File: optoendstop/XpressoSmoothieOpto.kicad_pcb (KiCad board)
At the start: 2 copper layers, 99.7 x 99.7 mm, 121 parts, among them J1 HEADER_4, J10 HEADER_3X2, J11 Pwr_in, J12 HEADER_4, J13 HEADER_4X2, J14 HEADER_3X2, J15 HEADER_4, J16 HEADER_4, J17 HEADER_4, J18 HEADER_4, J19 HEADER_2, J2 HEADER_4, J20 HEADER_2, J21 HEADER_2, J22 HEADER_2, J23 HEADER_4, J24 HEADER_4, J25 HEADER_4, J26 USB, J27 HEADER_4, J28 MICROSD-MOLEX, J3 HEADER_3, J4 HEADER_3X2, J5 HEADER_3X2, J6 LPCXPRESSO_GENERIC_HEADER, J7 HEADER_4, J8 HEADER_4, J9 HEADER_3X2, M1 LOGO_OSHW, M2 LOGO_OSHW, Q1 IRLB 8743, Q2 IRLB 8743, Q3 IRLB 8743, Q4 IRLB 8743, SW1 SW_PUSH, SW2 SW_PUSH, U1 POLOLU_A4988, U10 TC4422A, U11 TC4422A, U12 LM1117-3.3, U2 POLOLU_A4988, U3 POLOLU_A4988, U4 POLOLU_A4988, U5 POLOLU_A4988, U7 LM7809CT, U8 TC4422A, U9 TC4422A

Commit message: endstops_mod
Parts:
- moved C8 11.1 mm to (65.1, 117.5)
- moved C1 2.86 mm to (75.2, 117.5)
- moved J23 0.32 mm to (86.4, 109.5)
- moved J25 0.32 mm to (86.4, 113.3)
- moved J17 0.32 mm to (86.4, 105.7)
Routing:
- net Vin_rmot: track 317.8 -> 325.1 mm
- net GND: track 759.1 -> 755.0 mm
- net ZMIN: track 24.3 -> 23.5 mm
- net YMIN: track 25.8 -> 26.5 mm

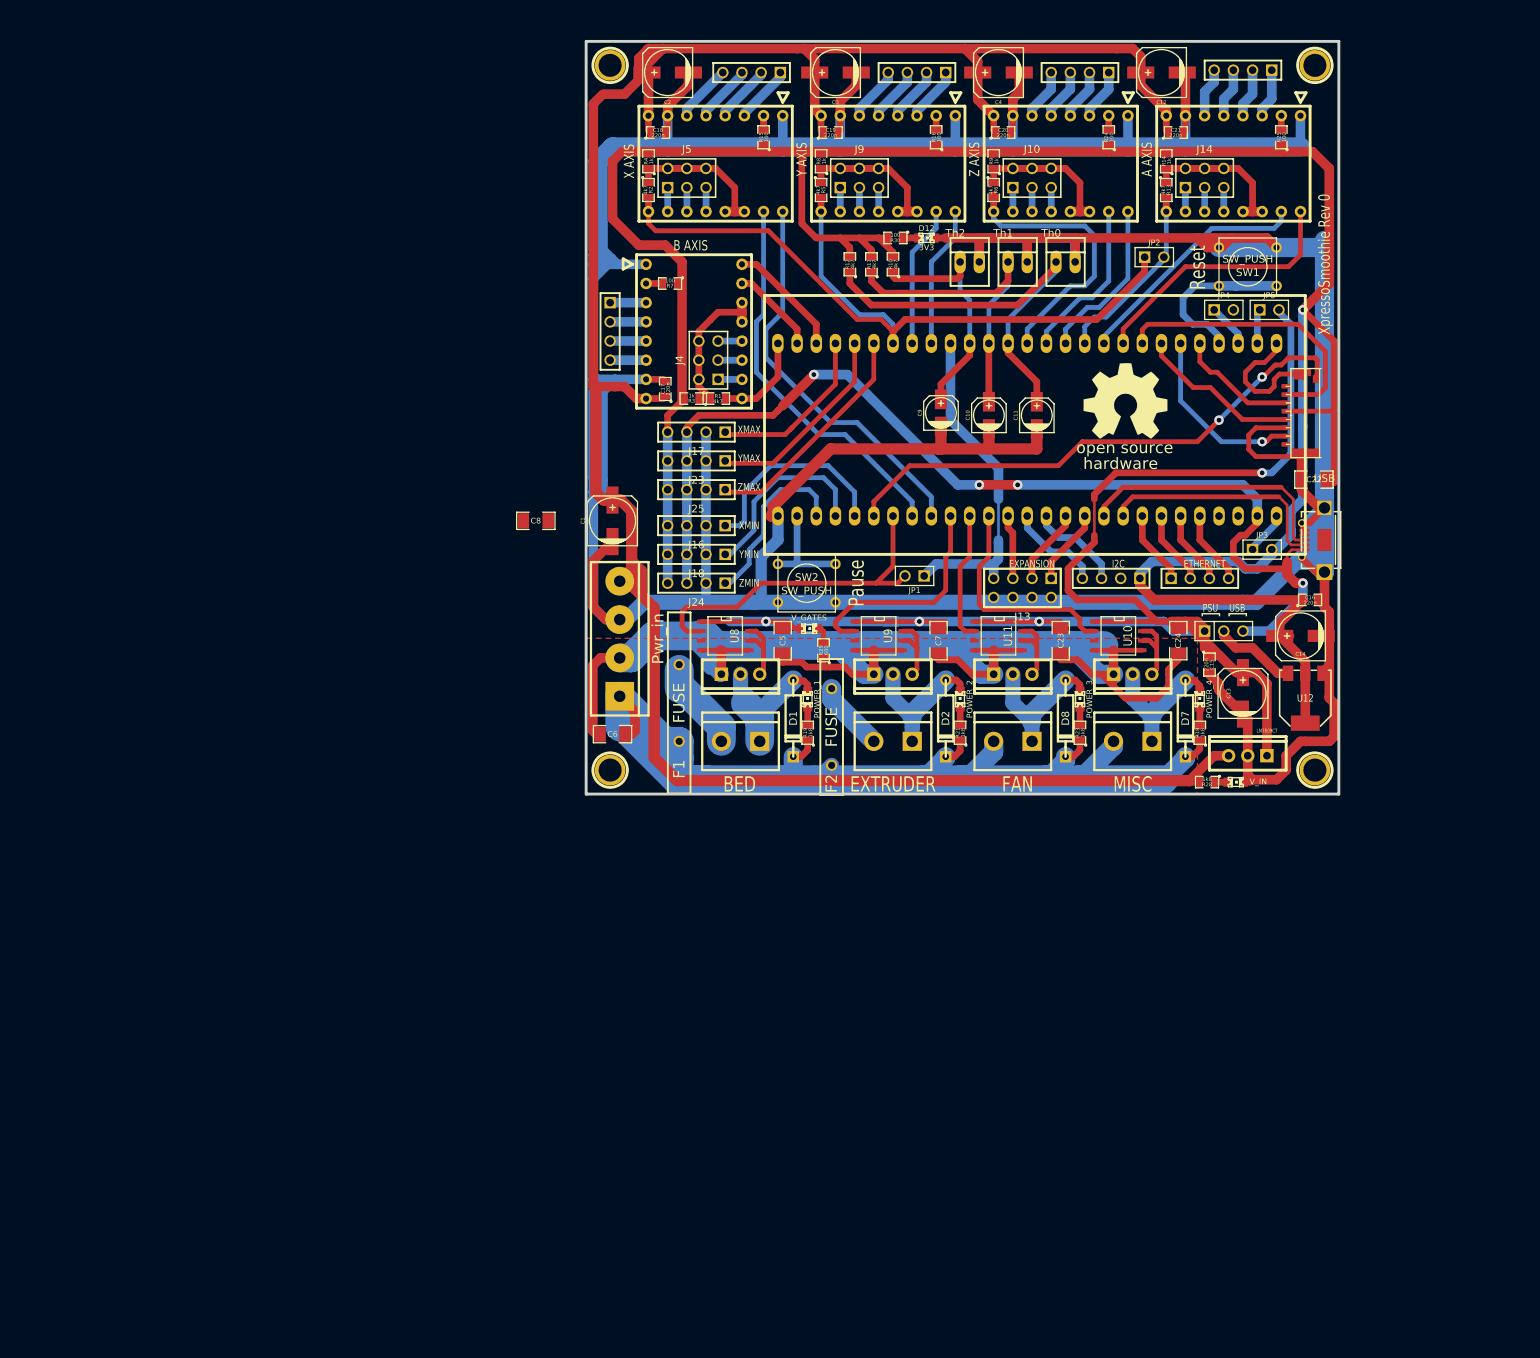
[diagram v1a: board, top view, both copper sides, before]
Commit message: opto_lib_and_mod
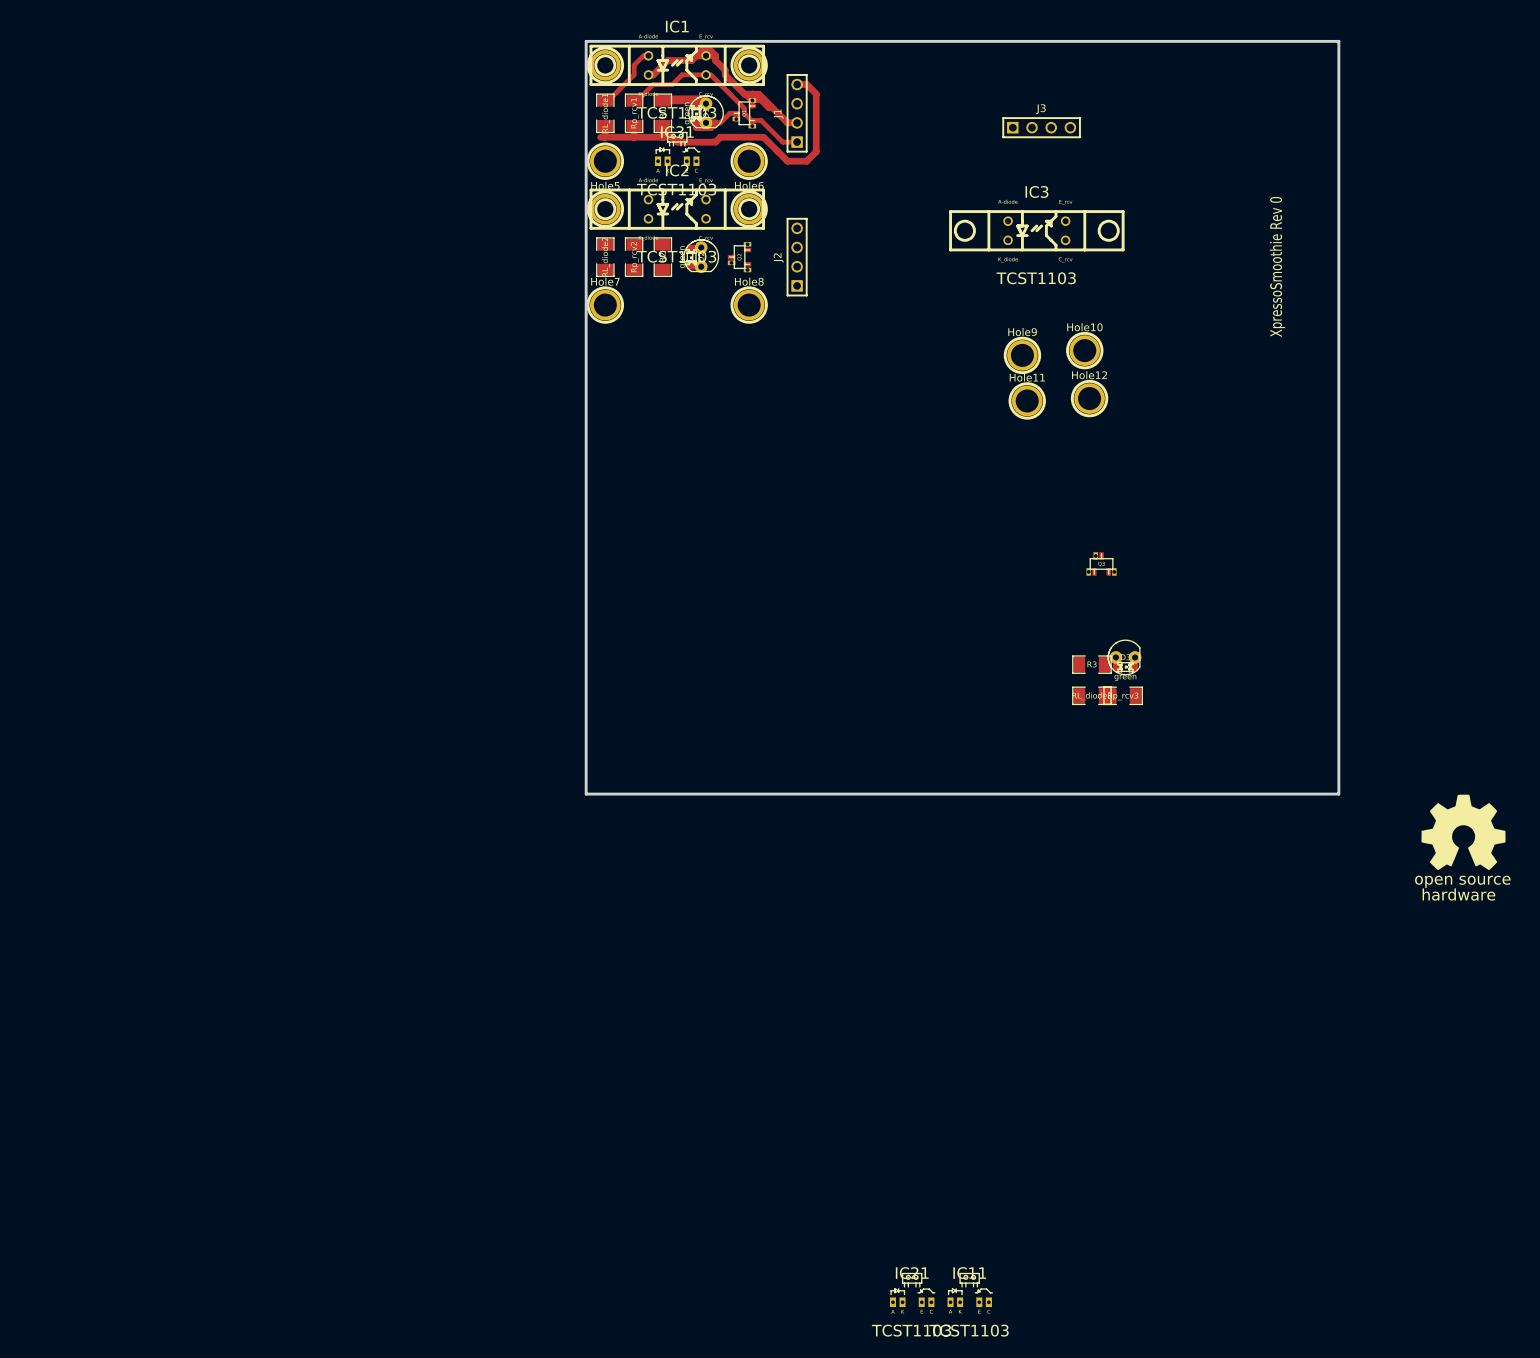
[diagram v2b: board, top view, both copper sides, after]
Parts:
- removed C1, C12, C13, C14, C2, C3, C4: 100u, c_elec_6.3x7.7
- removed C10, C11, C9: 10u, c_elec_4x5.3
- removed C15, C16, C17, C18, C19, C20, C21: 220n, SM0805
- removed C22: 1u, SM1206
- removed C23, C24, C5, C6, C7, C8: 1u/50v, SM1206
- removed D10: V_IN, LED-0805
- removed D11: V_GATES, LED-0805
- removed D12: 3V3, LED-0805
- removed D4: POWER_2, LED-0805
- removed D5: POWER_3, LED-0805
- removed D6: POWER_4, LED-0805
- removed D7, D8: 1N4007, DO-41
- removed F1: FUSE, MF-R1100
- removed F2: FUSE, MF-R500
- removed J10, J14, J4, J5, J9: HEADER_3X2, pin_array_3x2
- removed J11: Pwr_in, bornier4
- removed J12, J15, J16, J17, J18, J23, J24, J25, J27, J7, J8: HEADER_4, PIN_ARRAY_4x1
- removed J13: HEADER_4X2, pin_array_4x2
- removed J19, J20, J21, J22: HEADER_2, bornier2
- removed J26: USB, USB_MICRO_RMC
- removed J28: MICROSD-MOLEX, microsd-molex-47309
- removed J6: LPCXPRESSO_GENERIC_HEADER, LPCXPRESS0_GENERIC
- removed JP1, JP2, JP3, JP4, JP5: JUMPER-2, PIN_ARRAY_2X1
- removed Q4: IRLB 8743, TO220_VERT_C
- removed R10, R11, R12, R13, R5, R6: 4k7, SM0805
- removed R14, R4, R8, R9: 1k, SM0805
- removed R15, R16, R24, R25, R30, R7: 100, SM0805
- removed R18, R19, R21, R23, R28: 1k8, SM0805
- removed R29: 680, SM0805
- removed SW1, SW2: SW_PUSH, SW_PUSH_SMALL
- removed Th0, Th1, Th2: CONN_2, PINHEAD1-2
- removed U1, U2, U3, U4, U5: POLOLU_A4988, POLOLU
- removed U10, U11, U8, U9: TC4422A, SO8N
- removed U12: LM1117-3.3, SOT223_LM1117
- removed U7: LM7809CT, TO220_VERT_1117
- added Hole10: CONN_1, 1pin, F.Cu at (137.8, 94.9)
- added Hole11: CONN_1, 1pin, F.Cu at (130.2, 101.6)
- added Hole12: CONN_1, 1pin, F.Cu at (138.4, 101.3)
- added Hole5: CONN_1, 1pin, F.Cu at (74.3, 76.2)
- added Hole6: CONN_1, 1pin, F.Cu at (93.3, 76.2)
- added Hole7: CONN_1, 1pin, F.Cu at (74.3, 88.9)
- added Hole8: CONN_1, 1pin, F.Cu at (93.3, 88.9)
- added Hole9: CONN_1, 1pin, F.Cu at (129.5, 95.6)
- added IC1: TCST1103, TCST1103-2103, F.Cu at (83.8, 57.1)
- added IC11: TCST1103, TCRT1000, F.Cu at (122.6, 221.0)
- added IC2: TCST1103, TCST1103-2103, F.Cu at (83.8, 76.2)
- added IC21: TCST1103, TCRT1000, F.Cu at (114.9, 221.0)
- added IC3: TCST1103, TCST1103-2103, F.Cu at (131.4, 79.1)
- added IC31: TCST1103, TCRT1000, F.Cu at (83.8, 69.8)
- added RL_diode1: 68, SM1206, F.Cu at (74.3, 63.5)
- added RL_diode2: 68, SM1206, F.Cu at (74.3, 82.5)
- added RL_diode3: 68, SM1206, F.Cu at (138.7, 140.7)
- added Rp_rcv1: 1k5, SM1206, F.Cu at (78.1, 63.5)
- added Rp_rcv2: 1k5, SM1206, F.Cu at (78.1, 82.5)
- added Rp_rcv3: 1k5, SM1206, F.Cu at (142.9, 140.7)
- D1, D2: value 1N4007 -> green; footprint DO-41 -> LED-0805-3MM
- D3: value POWER_1 -> green; footprint LED-0805 -> LED-0805-3MM
- J3: value HEADER_3 -> HEADER_4; footprint PIN_ARRAY_3X1 -> PIN_ARRAY_4x1
- Q1, Q2, Q3: value IRLB 8743 -> BS108D; footprint TO220_VERT_C -> sot23-to92
- R1, R2: value 4k7 -> 150; footprint SM0805 -> SM1206
- R3: value 1k -> 150; footprint SM0805 -> SM1206
- moved Hole4 110.1 mm to (93.3, 69.8)
- moved M1 96.3 mm to (146.7, 185.4)
- moved D1 81.2 mm to (86.4, 63.5)
- moved Hole1 80.6 mm to (74.3, 69.8)
- moved Hole3 74.9 mm to (93.3, 57.1)
- moved Q1 74.3 mm to (92.7, 63.5), turned to 90 degrees
- moved M2 72.6 mm to (188.0, 158.8)
- moved J3 70.9 mm to (132.1, 65.4)
- moved D2 69.7 mm to (85.7, 82.5)
- moved R3 63.7 mm to (138.7, 136.5), turned to 0 degrees
- moved Q2 58.9 mm to (92.1, 82.5), turned to 90 degrees
- moved D3 42.3 mm to (143.2, 136.8), turned to 0 degrees
- moved R1 38.5 mm to (81.9, 63.5), turned to 270 degrees
- moved J1 38.1 mm to (99.7, 63.5), turned to 90 degrees
- moved J2 25.2 mm to (99.7, 82.5), turned to 90 degrees
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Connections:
- D1 pad 1: N-0000086 -> N-000004
- D1 pad 2: Vin_Hi_curr -> N-000003
- D2 pad 1: N-0000091 -> N-000005
- D2 pad 2: Vin_Hi_curr -> N-000006
- D3 pad 1: N-0000087 -> N-000007
- D3 pad 2: N-0000086 -> N-000008
- J1 pad 1: N-00000101 -> Signal1
- J1 pad 2: N-00000106 -> GND_1
- J1 pad 3: N-00000111 -> (no net)
- J1 pad 4: N-00000100 -> 3V3_1
- J2 pad 1: N-0000022 -> Signal2
- J2 pad 2: N-0000018 -> GND_2
- J2 pad 3: N-0000019 -> (no net)
- J2 pad 4: N-0000027 -> 3V3_2
- J3 pad 1: Vgates -> Signal3
- J3 pad 2: N-0000045 -> GND_3
- J3 pad 3: +5V -> (no net)
- Q1 pad D: N-0000086 -> N-000003
- Q1 pad G: N-0000084 -> Signal1
- Q1 pad S: GNDPWR -> GND_1
- Q2 pad D: N-0000091 -> N-000006
- Q2 pad G: N-0000092 -> Signal2
- Q2 pad S: GNDPWR -> GND_2
- Q3 pad D: N-0000088 -> N-000008
- Q3 pad G: N-0000089 -> Signal3
- Q3 pad S: GNDPWR -> GND_3
- R1 pad 1: N-00000113 -> N-000004
- R1 pad 2: B-EN -> 3V3_1
- R2 pad 1: N-0000023 -> N-000005
- R2 pad 2: X-EN -> 3V3_2
- R3 pad 1: N-00000113 -> N-000007
- R3 pad 2: +3.3VP -> 3V3_3
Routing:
- net GND: track 755.0 -> 0.00 mm
- net +3.3VP: track 353.5 -> 0.00 mm, vias 1 -> 0
- net Vin_rmot: track 325.1 -> 0.00 mm
- net Vgates: track 228.1 -> 0.00 mm, vias 4 -> 0
- net GNDPWR: track 197.7 -> 0.00 mm
- net Vin_Hi_curr: track 163.6 -> 0.00 mm
- net +5V: track 142.5 -> 0.00 mm, vias 4 -> 0
- net X-EN: track 108.7 -> 0.00 mm
- net SD_card_detect: track 71.3 -> 0.00 mm, vias 2 -> 0
- net THERM0: track 55.5 -> 0.00 mm
- net X-DIR: track 52.4 -> 0.00 mm
- net X-STEP: track 51.3 -> 0.00 mm
- net 3V3_1: track 0.00 -> 46.2 mm
- net POWER1: track 46.0 -> 0.00 mm
- net 18_P0.26AOUT: track 43.9 -> 0.00 mm
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- removed copper zone on F.Cu, net GNDPWR
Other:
- board text removed: "A AXIS"
- board text removed: "B AXIS"
- board text removed: "BED"
- board text removed: "ETHERNET"
- board text removed: "EXPANSION"
- board text removed: "EXTRUDER"
- board text removed: "FAN"
- board text removed: "I2C"
- board text removed: "MISC"
- board text removed: "PSU"
- board text removed: "Pause"
- board text removed: "Reset"
- board text removed: "USB"
- board text removed: "X AXIS"
- board text removed: "XMAX"
- board text removed: "XMIN"
- board text removed: "Y AXIS"
- board text removed: "YMAX"
- board text removed: "YMIN"
- board text removed: "Z AXIS"
- board text removed: "ZMAX"
- board text removed: "ZMIN"
- board text removed: "["

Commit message: oe_mod
oe_mod
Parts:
- moved M2 184.6 mm to (4.45, 179.1)
- moved IC11 168.3 mm to (83.8, 57.1)
- moved M1 152.7 mm to (0.64, 141.0)
- moved IC21 135.1 mm to (126.4, 86.4)
- moved Hole11 56.8 mm to (74.3, 111.8)
- moved D3 56.1 mm to (88.6, 124.1)
- moved R3 56.1 mm to (84.1, 123.8)
- moved RL_diode3 56.1 mm to (84.1, 128.0)
- moved Rp_rcv3 56.1 mm to (88.3, 128.0)
- moved Hole9 55.3 mm to (74.3, 97.8)
- moved IC31 52.3 mm to (126.4, 100.3)
- moved Q3 51.6 mm to (92.1, 104.1), turned to 90 degrees
- moved IC3 50.6 mm to (84.5, 97.8)
- moved J3 50.5 mm to (99.7, 104.1), turned to 90 degrees
- moved Hole12 46.3 mm to (93.3, 111.8)
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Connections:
- IC1 pad A/+: N-0000034 -> N-000001
- IC11 pad A/+: (no net) -> N-000001
- IC11 pad C/+: (no net) -> Signal1
- IC11 pad E/D: (no net) -> GND_1
- IC11 pad K/E: (no net) -> GND_1
- IC2 pad A/+: N-0000045 -> N-000005
- IC21 pad A/+: (no net) -> N-000005
- IC21 pad C/+: (no net) -> Signal2
- IC21 pad E/D: (no net) -> GND_2
- IC21 pad K/E: (no net) -> GND_2
- IC3 pad A/+: N-000009 -> N-000008
- IC31 pad A/+: (no net) -> N-000008
- IC31 pad C/+: (no net) -> Signal3
- IC31 pad E/D: (no net) -> GND_3
- IC31 pad K/E: (no net) -> GND_3
- RL_diode1 pad 1: N-0000034 -> N-000001
- RL_diode2 pad 1: N-0000045 -> N-000005
- RL_diode3 pad 1: N-000009 -> N-000008
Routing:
- net 3V3_1: track 46.2 -> 0.00 mm
- net GND_1: track 41.8 -> 13.4 mm
- net Signal1: track 27.8 -> 2.54 mm
- net N-0000016: track 10.8 -> 0.00 mm
- net N-0000021: track 10.3 -> 0.00 mm
- net N-0000034: track 8.93 -> 0.00 mm
- net N-000001: track 0.00 -> 2.54 mm
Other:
- outline, holes or cut-outs redrawn

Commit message: optoendstops
optoendstops
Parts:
- removed D2, D3: green, LED-0805-3MM
- removed Hole10, Hole11, Hole12, Hole5, Hole6, Hole7, Hole8, Hole9: CONN_1, 1pin
- removed IC2, IC3: TCST1103, TCST1103-2103
- removed IC21, IC31: TCST1103, TCRT1000
- removed J2, J3: HEADER_4, PIN_ARRAY_4x1
- removed M1: LOGO_OSHW, OSHW_large_silkscreen-back_70mm
- removed Q2, Q3: BS108D, sot23-to92
- removed R2, R3: 150, SM1206
- removed RL_diode2, RL_diode3: 68, SM1206
- removed Rp_rcv2, Rp_rcv3: 1k5, SM1206
- added JP1: JUMPER-3, SIL-3, F.Cu at (81.3, 61.0)
- moved M2 133.8 mm to (100.3, 85.7)
- moved J1 22.3 mm to (76.2, 66.0), turned to 90 degrees
- moved Hole3 19.7 mm to (88.3, 76.2), turned to 270 degrees
- moved Hole4 18.5 mm to (75.6, 76.2), turned to 270 degrees
- moved D1 17.1 mm to (83.8, 76.2), turned to 90 degrees
- moved Hole1 14.0 mm to (75.6, 57.1), turned to 270 degrees
- moved Hole2 14.0 mm to (88.3, 57.1), turned to 270 degrees
- moved RL_diode1 10.8 mm to (81.9, 57.1), turned to 180 degrees
- moved IC1 10.5 mm to (88.3, 66.7), turned to 270 degrees
- moved IC11 10.5 mm to (88.3, 66.7), turned to 270 degrees
- moved Rp_rcv1 9.52 mm to (82.5, 71.8), turned to 0 degrees
- moved R1 7.78 mm to (79.7, 75.6), turned to 90 degrees
- moved Q1 5.08 mm to (82.5, 67.9)
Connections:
- net 3V3_1 renamed 3.3V
- net GND_1 renamed GND
- J1 pad 3: (no net) -> 5V
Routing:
- net 3.3V: track 0.00 -> 46.5 mm
- net GND: track 13.4 -> 42.4 mm
- net Signal1: track 2.54 -> 24.9 mm
- net N-000006: track 2.54 -> 14.3 mm
- net 5V: track 0.00 -> 9.94 mm
- net N-000002: track 0.00 -> 7.95 mm
- net N-000001: track 0.00 -> 3.28 mm
- added copper zone on B.Cu, net GND
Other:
- outline, holes or cut-outs redrawn
- board text added: "x4"
- board text added: "x5"
- board text removed: "XpressoSmoothie Rev 0"

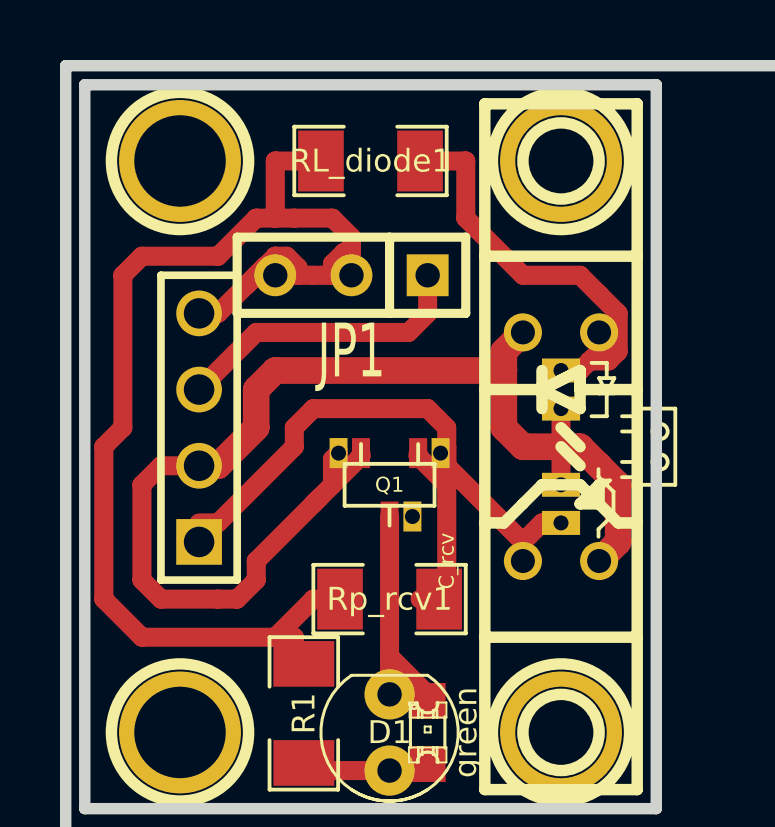
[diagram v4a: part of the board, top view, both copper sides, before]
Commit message: optod-rem-jumper
removed jumper
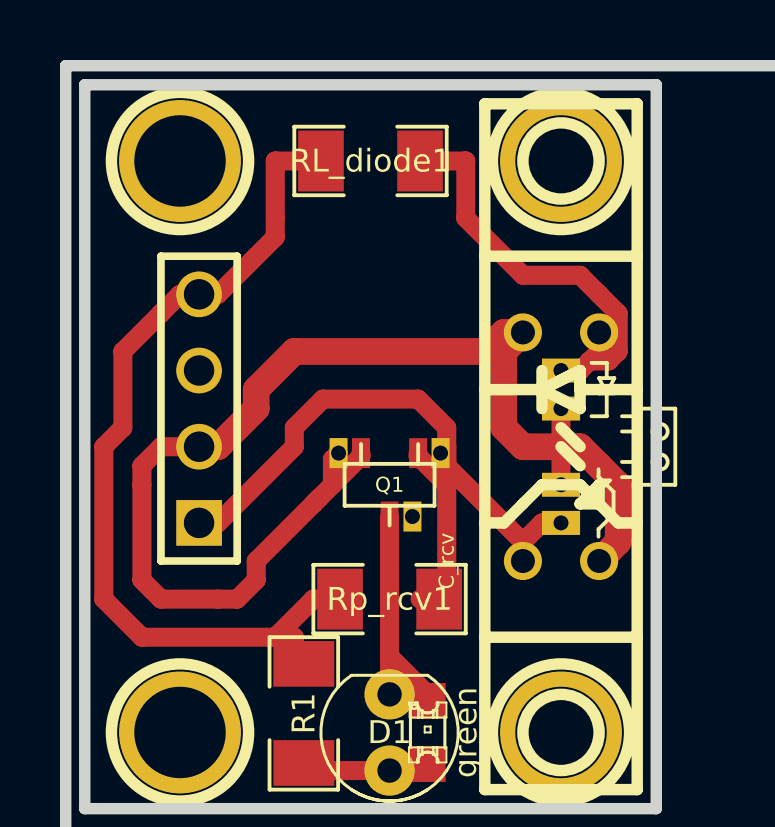
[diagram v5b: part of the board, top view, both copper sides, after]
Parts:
- removed JP1: JUMPER-3, SIL-3
- moved J1 0.64 mm to (76.2, 65.4)
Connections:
- J1 pad 3: 5V -> (no net)
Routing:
- net 3.3V: track 46.5 -> 29.7 mm
- net 5V: track 9.94 -> 0.00 mm
- net GND: track 42.4 -> 43.5 mm
